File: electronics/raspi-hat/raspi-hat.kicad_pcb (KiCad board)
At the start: 4 copper layers, 65 x 56 mm, 25 parts, among them J1 12V from battery, J2 5V to other boards, J3 40HAT, J4 CAN, Q1 DMG2305UX, Q2 DMMT5401, U1 MCP2515-xSO, U3 MAX33012EASA+, U4 MYMGA5R04RELA5RA, Y1 Crystal_GND24_Small

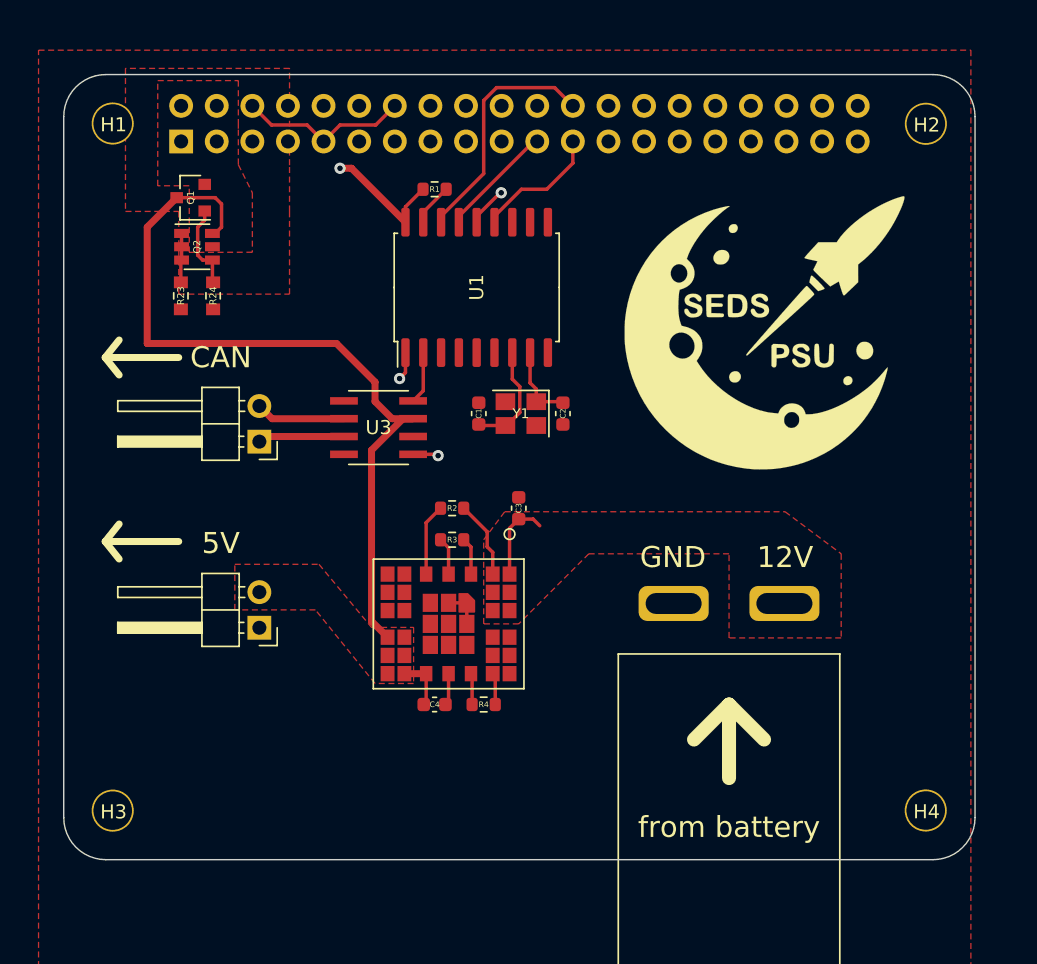
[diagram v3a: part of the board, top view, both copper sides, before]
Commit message: Add filled backplane to raspberry pi hat
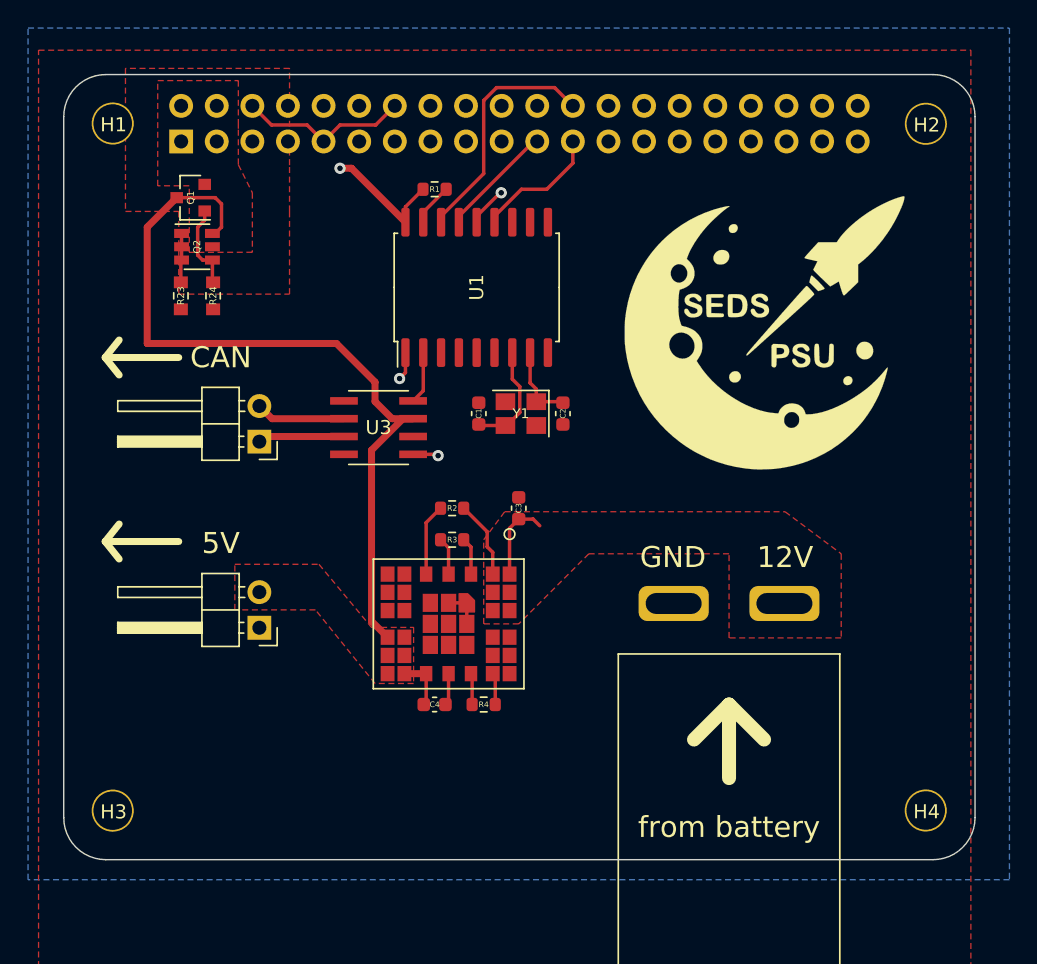
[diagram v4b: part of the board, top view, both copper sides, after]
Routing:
- added copper zone on B.Cu, net (none)
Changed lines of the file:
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@@
+    )
+  )
+  (zone (net 0) (net_name "") (layer "B.Cu") (hatch edge 0.508)
+    (connect_pads (clearance 0.4))
+    (min_thickness 0.254) (filled_areas_thickness no)
+    (fill yes (thermal_gap 0.508) (thermal_bridge_width 0.508))
+    (polygon
+      (pts
+        (xy 146 118.25)
+        (xy 76 118.25)
+        (xy 76 57.5)
+        (xy 146 57.5)
+      )
     )
   )
